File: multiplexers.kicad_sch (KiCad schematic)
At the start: 12 parts, among them U2 74HC4067, U3 74HC4067, U4 74HC4067, U5 74HC4067, U6 74HC4067, U7 74HC4067

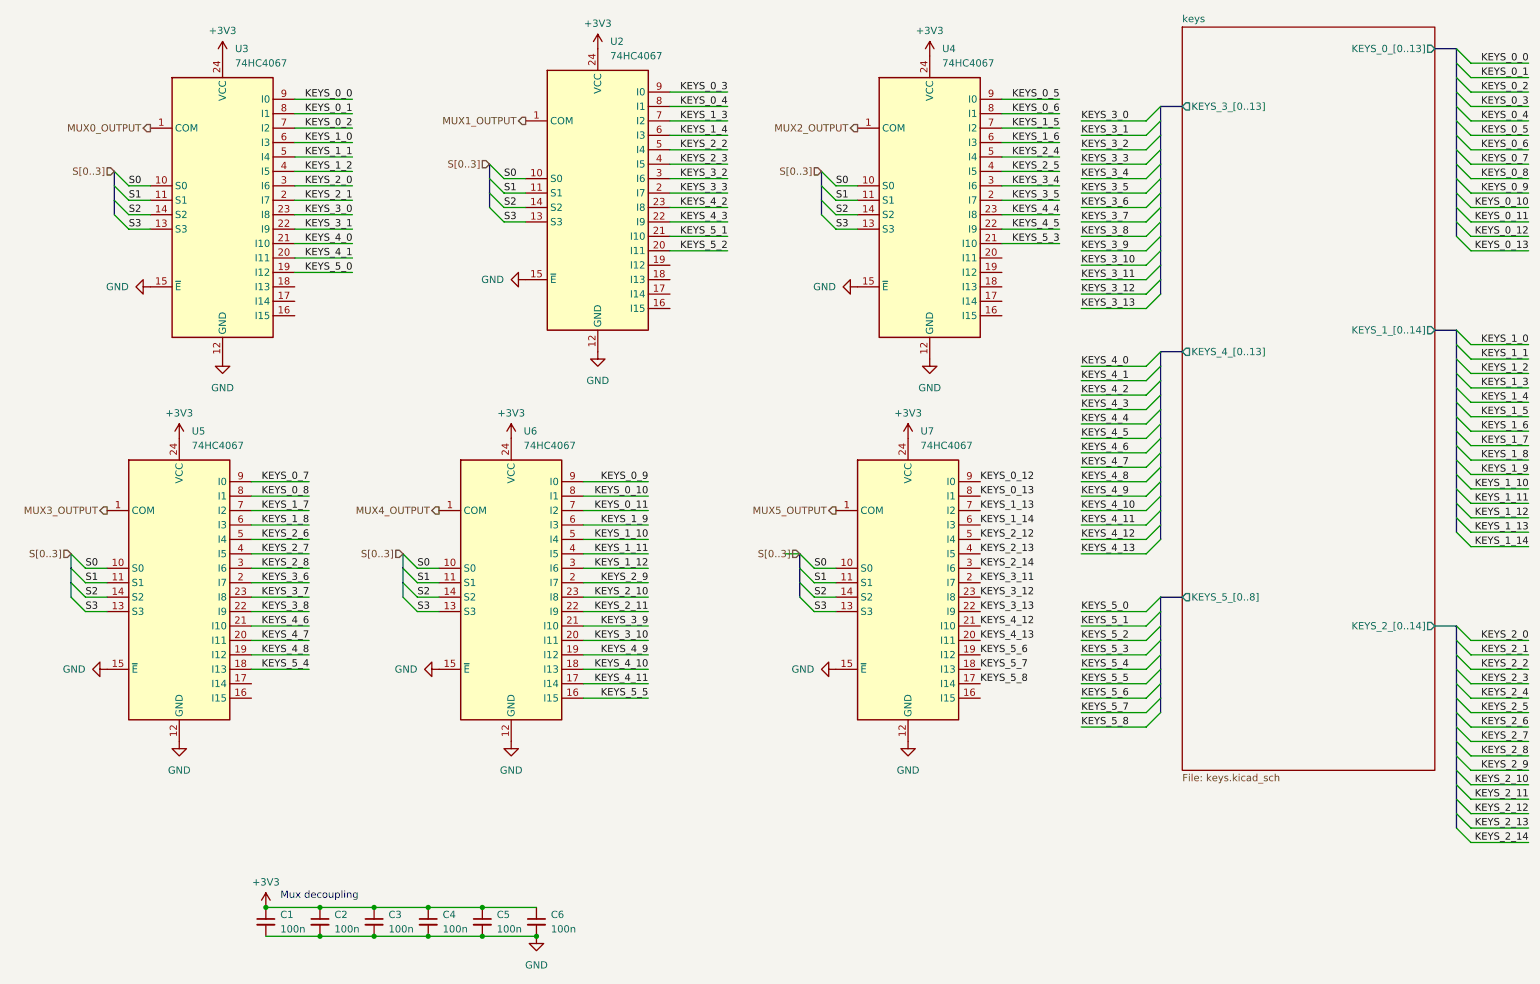
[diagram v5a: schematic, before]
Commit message: Routed a lot of the pcb, additionally fixed issues with wrong layout
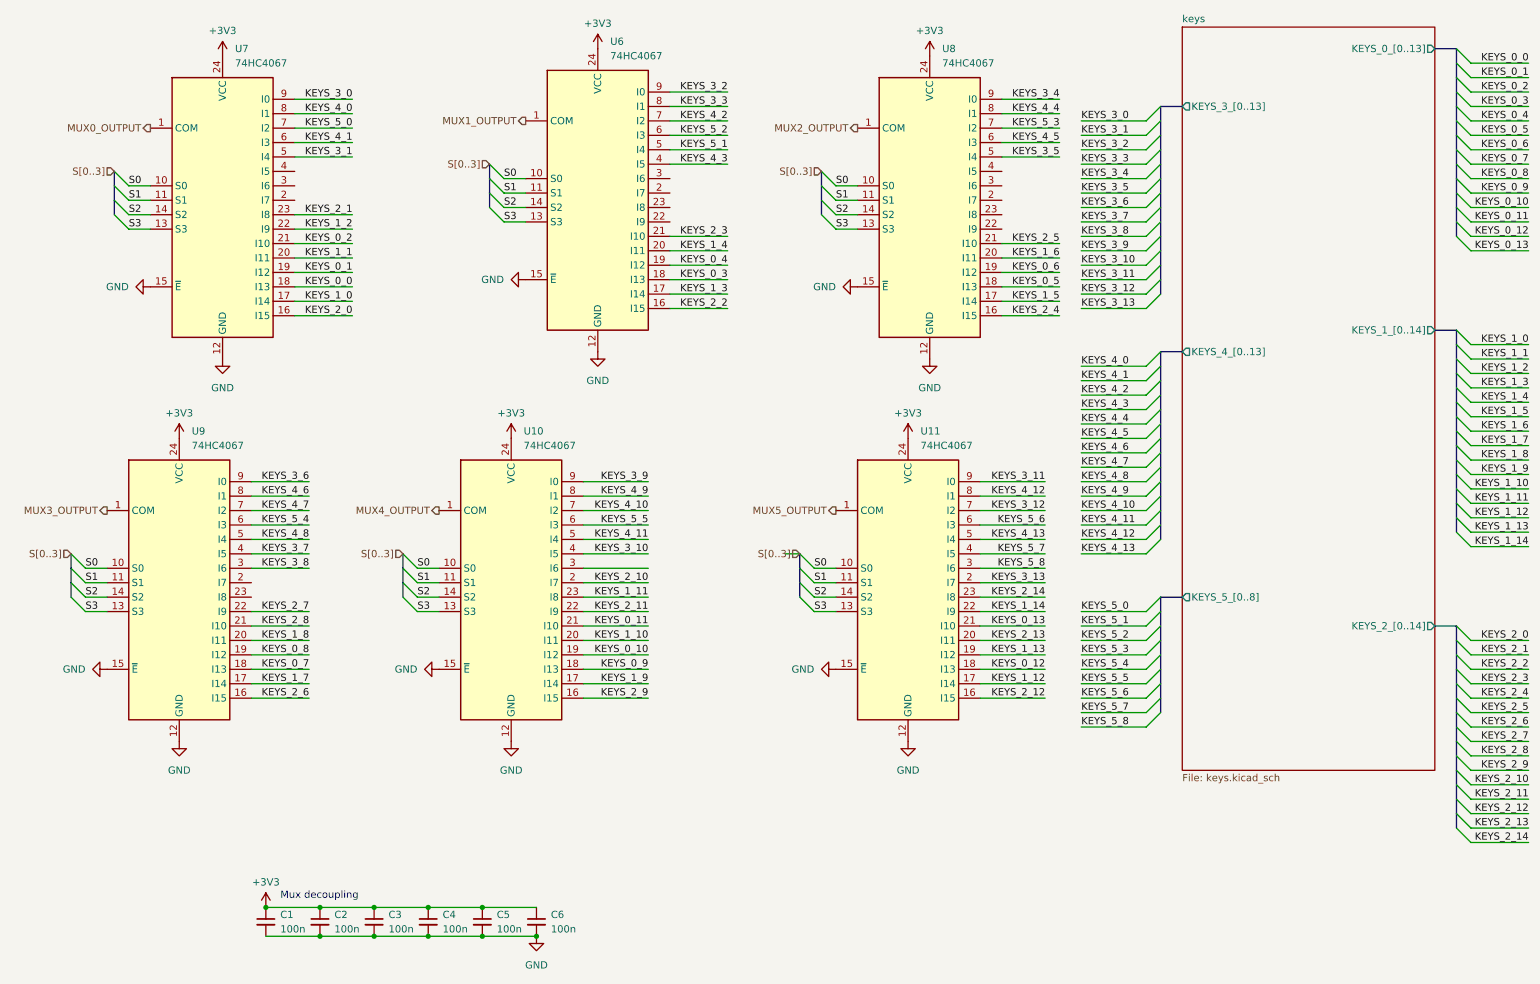
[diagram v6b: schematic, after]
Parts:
- renumbered U6 to U10, U7 to U11, U2 to U6, U3 to U7, U4 to U8, U5 to U9
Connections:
- net KEYS_0_0: now also U7.18 (I13); no longer U7.9 (I0)
- net KEYS_0_1: now also U7.19 (I12); no longer U7.8 (I1)
- net KEYS_0_10: now also U10.19 (I12); no longer U10.8 (I1)
- net KEYS_0_11: now also U10.21 (I10); no longer U10.7 (I2)
- net KEYS_0_12: now also U11.18 (I13); no longer U11.9 (I0)
- net KEYS_0_13: now also U11.21 (I10); no longer U11.8 (I1)
- net KEYS_0_2: now also U7.21 (I10); no longer U7.7 (I2)
- net KEYS_0_3: now also U6.18 (I13); no longer U6.9 (I0)
- net KEYS_0_4: now also U6.19 (I12); no longer U6.8 (I1)
- net KEYS_0_5: now also U8.18 (I13); no longer U8.9 (I0)
- net KEYS_0_6: now also U8.19 (I12); no longer U8.8 (I1)
- net KEYS_0_7: now also U9.18 (I13); no longer U9.9 (I0)
- net KEYS_0_8: now also U9.19 (I12); no longer U9.8 (I1)
- net KEYS_0_9: now also U10.18 (I13); no longer U10.9 (I0)
- net KEYS_1_0: now also U7.17 (I14); no longer U7.6 (I3)
- net KEYS_1_1: now also U7.20 (I11); no longer U7.5 (I4)
- net KEYS_1_10: now also U10.20 (I11); no longer U10.5 (I4)
- net KEYS_1_11: now also U10.23 (I8); no longer U10.4 (I5)
- net KEYS_1_12: now also U11.17 (I14); no longer U10.3 (I6)
- net KEYS_1_13: now also U11.19 (I12); no longer U11.7 (I2)
- net KEYS_1_14: now also U11.22 (I9); no longer U11.6 (I3)
- net KEYS_1_2: now also U7.22 (I9); no longer U7.4 (I5)
- net KEYS_1_3: now also U6.17 (I14); no longer U6.7 (I2)
- net KEYS_1_4: now also U6.20 (I11); no longer U6.6 (I3)
- net KEYS_1_5: now also U8.17 (I14); no longer U8.7 (I2)
- net KEYS_1_6: now also U8.20 (I11); no longer U8.6 (I3)
- net KEYS_1_7: now also U9.17 (I14); no longer U9.7 (I2)
- net KEYS_1_8: now also U9.20 (I11); no longer U9.6 (I3)
- net KEYS_1_9: now also U10.17 (I14); no longer U10.6 (I3)
- net KEYS_2_0: now also U7.16 (I15); no longer U7.3 (I6)
- net KEYS_2_1: now also U7.23 (I8); no longer U7.2 (I7)
- net KEYS_2_10: now also U10.2 (I7); no longer U10.23 (I8)
- net KEYS_2_12: now also U11.16 (I15); no longer U11.5 (I4)
- net KEYS_2_13: now also U11.20 (I11); no longer U11.4 (I5)
- net KEYS_2_14: now also U11.23 (I8); no longer U11.3 (I6)
- net KEYS_2_2: now also U6.16 (I15); no longer U6.5 (I4)
- net KEYS_2_3: now also U6.21 (I10); no longer U6.4 (I5)
- net KEYS_2_4: now also U8.16 (I15); no longer U8.5 (I4)
- net KEYS_2_5: now also U8.21 (I10); no longer U8.4 (I5)
- net KEYS_2_6: now also U9.16 (I15); no longer U9.5 (I4)
- net KEYS_2_7: now also U9.22 (I9); no longer U9.4 (I5)
- net KEYS_2_8: now also U9.21 (I10); no longer U9.3 (I6)
- net KEYS_2_9: now also U10.16 (I15); no longer U10.2 (I7)
- net KEYS_3_0: now also U7.9 (I0); no longer U7.23 (I8)
- net KEYS_3_1: now also U7.5 (I4); no longer U7.22 (I9)
- net KEYS_3_10: now also U10.4 (I5); no longer U10.20 (I11)
- net KEYS_3_11: now also U11.9 (I0); no longer U11.2 (I7)
- net KEYS_3_12: now also U11.7 (I2); no longer U11.23 (I8)
- net KEYS_3_13: now also U11.2 (I7); no longer U11.22 (I9)
- net KEYS_3_2: now also U6.9 (I0); no longer U6.3 (I6)
- net KEYS_3_3: now also U6.8 (I1); no longer U6.2 (I7)
- net KEYS_3_4: now also U8.9 (I0); no longer U8.3 (I6)
- net KEYS_3_5: now also U8.5 (I4); no longer U8.2 (I7)
- net KEYS_3_6: now also U9.9 (I0); no longer U9.2 (I7)
- net KEYS_3_7: now also U9.4 (I5); no longer U9.23 (I8)
- net KEYS_3_8: now also U9.3 (I6); no longer U9.22 (I9)
- net KEYS_3_9: now also U10.9 (I0); no longer U10.21 (I10)
- net KEYS_4_0: now also U7.8 (I1); no longer U7.21 (I10)
- net KEYS_4_1: now also U7.6 (I3); no longer U7.20 (I11)
- net KEYS_4_10: now also U10.7 (I2); no longer U10.18 (I13)
- net KEYS_4_11: now also U10.5 (I4); no longer U10.17 (I14)
- net KEYS_4_12: now also U11.8 (I1); no longer U11.21 (I10)
- net KEYS_4_13: now also U11.5 (I4); no longer U11.20 (I11)
- net KEYS_4_2: now also U6.7 (I2); no longer U6.23 (I8)
- net KEYS_4_3: now also U6.4 (I5); no longer U6.22 (I9)
- net KEYS_4_4: now also U8.8 (I1); no longer U8.23 (I8)
- net KEYS_4_5: now also U8.6 (I3); no longer U8.22 (I9)
- net KEYS_4_6: now also U9.8 (I1); no longer U9.21 (I10)
- net KEYS_4_7: now also U9.7 (I2); no longer U9.20 (I11)
- net KEYS_4_8: now also U9.5 (I4); no longer U9.19 (I12)
- net KEYS_4_9: now also U10.8 (I1); no longer U10.19 (I12)
- net KEYS_5_0: now also U7.7 (I2); no longer U7.19 (I12)
- net KEYS_5_1: now also U6.5 (I4); no longer U6.21 (I10)
- net KEYS_5_2: now also U6.6 (I3); no longer U6.20 (I11)
- net KEYS_5_3: now also U8.7 (I2); no longer U8.21 (I10)
- net KEYS_5_4: now also U9.6 (I3); no longer U9.18 (I13)
- net KEYS_5_5: now also U10.6 (I3); no longer U10.16 (I15)
- net KEYS_5_6: now also U11.6 (I3); no longer U11.19 (I12)
- net KEYS_5_7: now also U11.4 (I5); no longer U11.18 (I13)
- net KEYS_5_8: now also U11.3 (I6); no longer U11.17 (I14)

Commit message: Finished routing all switches
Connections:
- net KEYS_0_0: now also U7.21 (I10); no longer U7.18 (I13)
- net KEYS_0_1: now also U7.23 (I8); no longer U7.19 (I12)
- net KEYS_0_10: now also U10.16 (I15); no longer U10.19 (I12)
- net KEYS_0_11: now also U10.19 (I12); no longer U10.21 (I10)
- net KEYS_0_13: now also U11.19 (I12); no longer U11.21 (I10)
- net KEYS_0_2: now also U7.20 (I11); no longer U7.21 (I10)
- net KEYS_0_3: now also U6.21 (I10); no longer U6.18 (I13)
- net KEYS_0_4: now also U6.20 (I11); no longer U6.19 (I12)
- net KEYS_0_5: now also U8.21 (I10); no longer U8.18 (I13)
- net KEYS_0_6: now also U8.20 (I11); no longer U8.19 (I12)
- net KEYS_0_7: now also U9.21 (I10); no longer U9.18 (I13)
- net KEYS_0_8: now also U9.22 (I9); no longer U9.19 (I12)
- net KEYS_1_0: now also U7.19 (I12); no longer U7.17 (I14)
- net KEYS_1_1: now also U7.22 (I9); no longer U7.20 (I11)
- net KEYS_1_10: now also U10.17 (I14); no longer U10.20 (I11)
- net KEYS_1_11: now also U10.21 (I10); no longer U10.23 (I8)
- net KEYS_1_12: now also U11.20 (I11); no longer U11.17 (I14)
- net KEYS_1_13: now also U11.16 (I15); no longer U11.19 (I12)
- net KEYS_1_14: now also U11.21 (I10); no longer U11.22 (I9)
- net KEYS_1_2: now also U7.18 (I13); no longer U7.22 (I9)
- net KEYS_1_3: now also U6.19 (I12); no longer U6.17 (I14)
- net KEYS_1_4: now also U6.18 (I13); no longer U6.20 (I11)
- net KEYS_1_5: now also U8.19 (I12); no longer U8.17 (I14)
- net KEYS_1_6: now also U8.18 (I13); no longer U8.20 (I11)
- net KEYS_1_7: now also U9.19 (I12); no longer U9.17 (I14)
- net KEYS_1_9: now also U10.20 (I11); no longer U10.17 (I14)
- net KEYS_2_0: now also U7.17 (I14); no longer U7.16 (I15)
- net KEYS_2_1: now also U7.16 (I15); no longer U7.23 (I8)
- net KEYS_2_10: now also U10.8 (I1); no longer U10.2 (I7)
- net KEYS_2_11: now also U10.23 (I8); no longer U10.22 (I9)
- net KEYS_2_12: now also U11.22 (I9); no longer U11.16 (I15)
- net KEYS_2_13: now also U11.17 (I14); no longer U11.20 (I11)
- net KEYS_2_2: now also U6.17 (I14); no longer U6.16 (I15)
- net KEYS_2_3: now also U6.16 (I15); no longer U6.21 (I10)
- net KEYS_2_4: now also U8.17 (I14); no longer U8.16 (I15)
- net KEYS_2_5: now also U8.16 (I15); no longer U8.21 (I10)
- net KEYS_2_6: now also U9.17 (I14); no longer U9.16 (I15)
- net KEYS_2_7: now also U9.16 (I15); no longer U9.22 (I9)
- net KEYS_2_8: now also U9.18 (I13); no longer U9.21 (I10)
- net KEYS_2_9: now also U10.22 (I9); no longer U10.16 (I15)
- net KEYS_3_1: now also U7.8 (I1); no longer U7.5 (I4)
- net KEYS_3_10: now also U10.6 (I3); no longer U10.4 (I5)
- net KEYS_3_11: now also U11.8 (I1); no longer U11.9 (I0)
- net KEYS_3_13: now also U11.6 (I3); no longer U11.2 (I7)
- net KEYS_3_5: now also U8.8 (I1); no longer U8.5 (I4)
- net KEYS_3_7: now also U9.6 (I3); no longer U9.4 (I5)
- net KEYS_3_8: now also U9.8 (I1); no longer U9.3 (I6)
- net KEYS_4_0: now also U7.7 (I2); no longer U7.8 (I1)
- net KEYS_4_10: now also U10.5 (I4); no longer U10.7 (I2)
- net KEYS_4_11: now also U10.4 (I5); no longer U10.5 (I4)
- net KEYS_4_12: now also U11.9 (I0); no longer U11.8 (I1)
- net KEYS_4_13: now also U11.3 (I6); no longer U11.5 (I4)
- net KEYS_4_4: now also U8.7 (I2); no longer U8.8 (I1)
- net KEYS_4_6: now also U9.7 (I2); no longer U9.8 (I1)
- net KEYS_4_7: now also U9.5 (I4); no longer U9.7 (I2)
- net KEYS_4_8: now also U9.4 (I5); no longer U9.5 (I4)
- net KEYS_4_9: now also U10.7 (I2); no longer U10.8 (I1)
- net KEYS_5_0: now also U7.5 (I4); no longer U7.7 (I2)
- net KEYS_5_3: now also U8.5 (I4); no longer U8.7 (I2)
- net KEYS_5_4: now also U9.3 (I6); no longer U9.6 (I3)
- net KEYS_5_5: now also U10.3 (I6); no longer U10.6 (I3)
- net KEYS_5_6: now also U11.5 (I4); no longer U11.6 (I3)
- net KEYS_5_7: now also U11.2 (I7); no longer U11.4 (I5)
- net KEYS_5_8: now also U11.4 (I5); no longer U11.3 (I6)
